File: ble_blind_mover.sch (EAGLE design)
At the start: 64 parts, among them J1 105017-0001, Q1 DMG6968U-7, Q2 DMG6968U-7, U1 MCP7940N-I/SN, U2 YJ-14015, U3 VIPER012LS, U4 MIC5205-3.3YM5-TR, Y1 LFXTAL016178

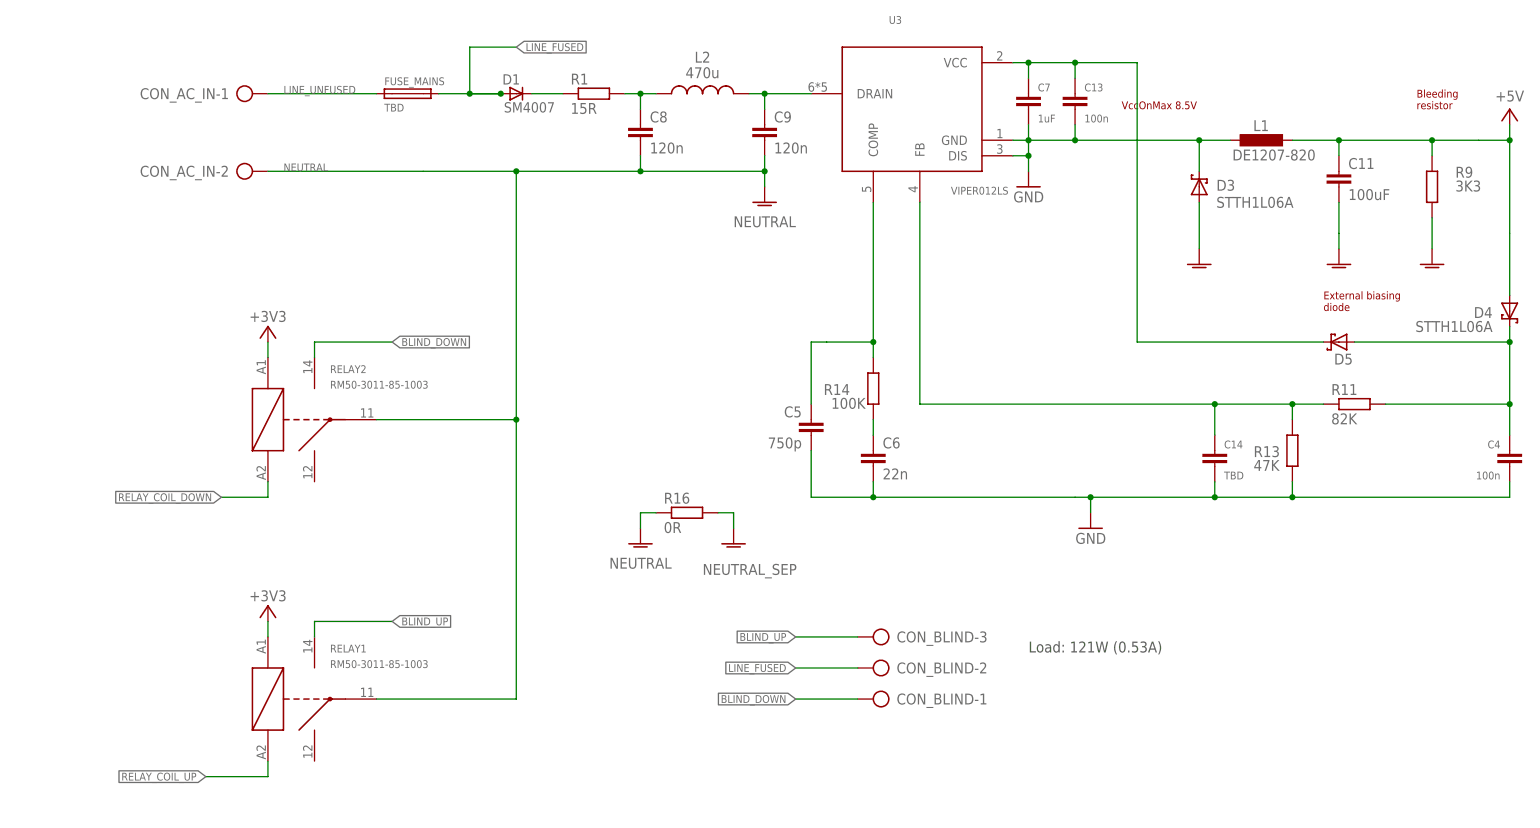
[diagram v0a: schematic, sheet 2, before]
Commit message: - Get rid from Viper PSU in favour of a Meanwell module - Make the contours to fit in a Kradex Z21 box
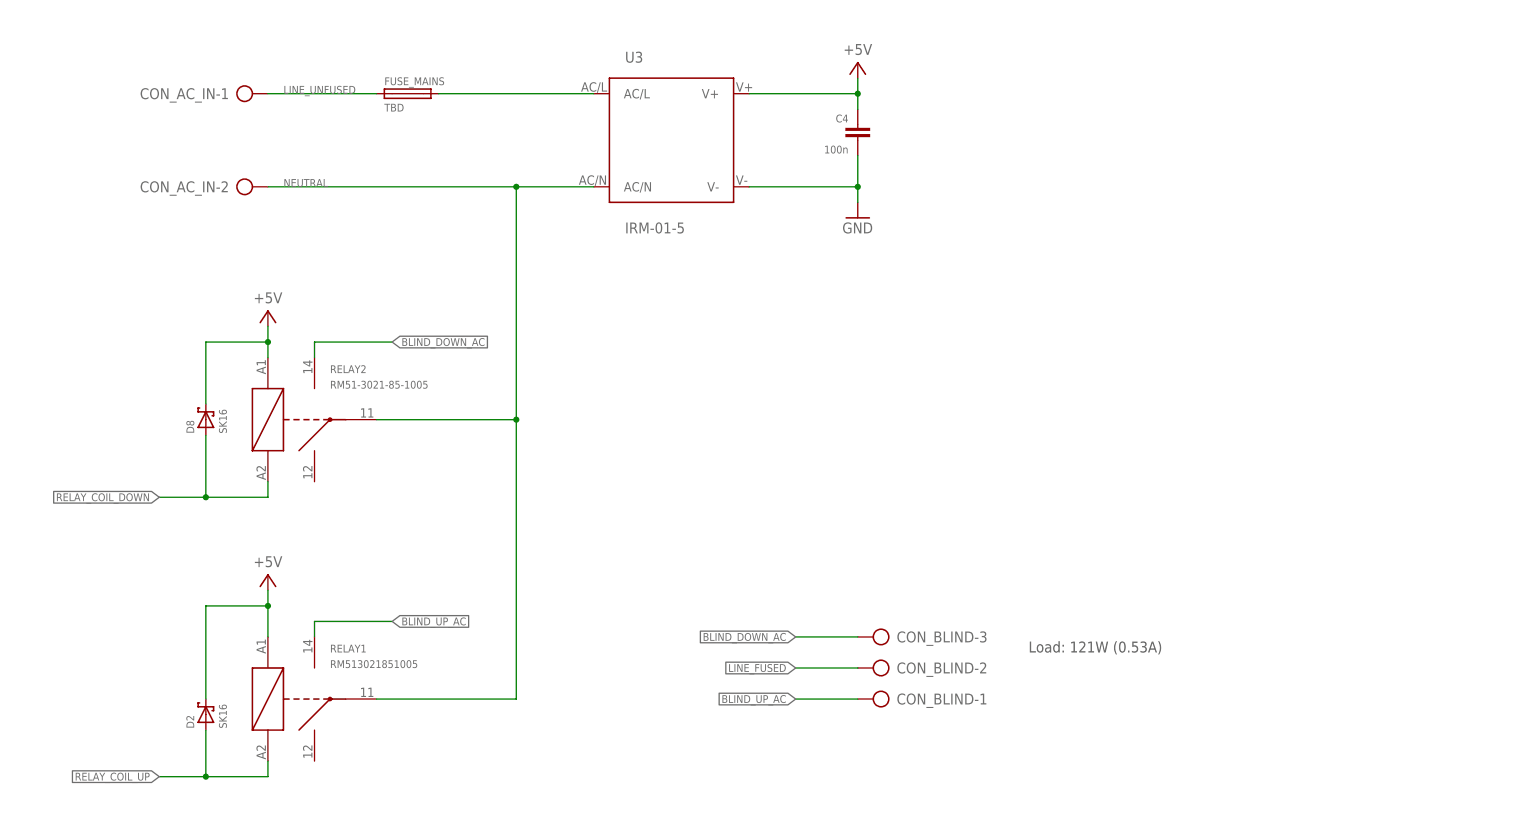
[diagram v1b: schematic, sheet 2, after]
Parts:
- removed C10, C7: 1uF, rcl:C-EUC0603
- removed C11: 100uF, rcl:C-EUC1812
- removed C13: 100n, rcl:C-EUC0603
- removed C14: TBD, rcl:C-EUC0603
- removed C5: 750p, rcl:C-EUC0603
- removed C6: 22n, rcl:C-EUC0603
- removed C8, C9: 120n, rcl:C-EU150-064X183
- removed D1: SM4007, _hhn_diodes_smd:SM4007
- removed D3, D4, D6: STTH1L06A, xCommonLib:SCHOTTKY_DIODESMA
- removed D5: (no value), diode_:SCHOTTKY-DIODESOD123
- removed J1: 105017-0001, 105017-0001:105017-0001
- removed JP1, JP2: (no value), pinhead:PINHD-1X2
- removed L1: DE1207-820, ferrocore:DE1207-820
- removed L2: 470u, SparkFun:INDUCTOR1210
- removed R1: 15R, rcl:R-EU_M1206
- removed R11: 82K, rcl:R-EU_R0603
- removed R13: 47K, rcl:R-EU_R0603
- removed R14: 100K, rcl:R-EU_R0603
- removed R16: 0R, rcl:R-EU_0207/7
- removed R9: 3K3, rcl:R-EU_R1206
- added C20, C21: 10n, rcl:C-EUC0603
- added D2, D8: SK16, diode:SCHOTTKY-DIODESK12
- added R18, R19: TBD, rcl:R-EU_R0603
- RELAY1: value RM50-3011-85-1003 -> RM513021851005; OC_TME RM50-P-03 -> RM513021851005
- RELAY2: value RM50-3011-85-1003 -> RM51-3021-85-1005; OC_TME RM50-P-03 -> RM513021851005
- U3: value VIPER012LS -> IRM-01-5; device st_viper:VIPER012LS -> meanwell_irm_v7:IRM_01/02IRM_01/02; OC_TME (none) -> IRM-01-5
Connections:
- removed net BLIND_DOWN: CON_BLIND-1.KL, RELAY2.14
- removed net BLIND_UP: CON_BLIND-3.KL, RELAY1.14
- removed net LINE_FILTERED: C9.1, L2.2, U3.DRAIN
- removed net LINE_RECTIFIED: D1.C, R1.1
- removed net LINE_RECTIFIED_R: C8.1, L2.1, R1.2
- removed net NEUTRAL_SEP: C11.2, D3.A, R16.2, R9.1
- removed net VIPER_COMP: C5.1, R14.2, U3.COMP
- removed net VIPER_COMP_MID: C6.1, R14.1
- removed net VIPER_FB: C14.1, R11.1, R13.2, U3.FB
- removed net VIPER_PRE_FB: C4.1, D4.C, D5.A, R11.2
- removed net VIPER_VCC: C13.1, C7.1, D5.C, U3.VCC
- removed net VUSB: D6.A, J1.VUSB
- new net BLIND_DOWN_AC: CON_BLIND-3.KL, RELAY2.14
- new net BLIND_UP_AC: CON_BLIND-1.KL, RELAY1.14
- new net BTN_DOWN_R: C20.1, R18.1, S4.S, S4.S1
- new net BTN_UP_R: C21.1, R19.1, S3.S, S3.S1
- net +3V3: no longer JP1.1, RELAY1.A1, RELAY2.A1
- net +5V: now also C4.1, D2.C, D8.C, RELAY1.A1, RELAY2.A1, U3.V+; no longer C10.1, C11.1, D4.A, D6.C, JP2.1, L1.2, R9.2
- net BTN_DOWN: now also R18.2, U2.P0.21; no longer S4.S, S4.S1, U2.P0.16
- net BTN_UP: now also R19.2; no longer S3.S, S3.S1
- net GND: now also C20.2, C21.2, U3.V-; no longer C10.2, C13.2, C14.2, C5.2, C6.2, C7.2, D3.C, J1.GND, J1.HOLES, J1.PADS, JP1.2, JP2.2, L1.1, R13.1, U3.DIS, U3.GND
- net LINE_FUSED: now also U3.AC/L; no longer D1.A
- net NEUTRAL: now also U3.AC/N; no longer C8.2, C9.2, R16.1
- net RELAY_COIL_DOWN: now also D8.A
- net RELAY_COIL_UP: now also D2.A
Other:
- note added: "+3V3"
- note added: "+5V"
- note added: "230V - 5V AC/DC converter"
- note added: "2x 5V Relay"
- note removed: "2 Relays"
- note removed: "230V - 3V3 AC/DC converter"
- note removed: "3V3"
- note removed: "Bleeding resistor"
- note removed: "External biasing diode"
- note removed: "PI filter, 1/2 bridge rectifier"
- note removed: "VccOnMax 8.5V"
- note removed: "uUSB socket"
- moved on the sheet: C12, C15, C17, C19, C4, CON_AC_IN-2, JP3, R15, R17, U1, Y1

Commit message: MOved to a triac based design
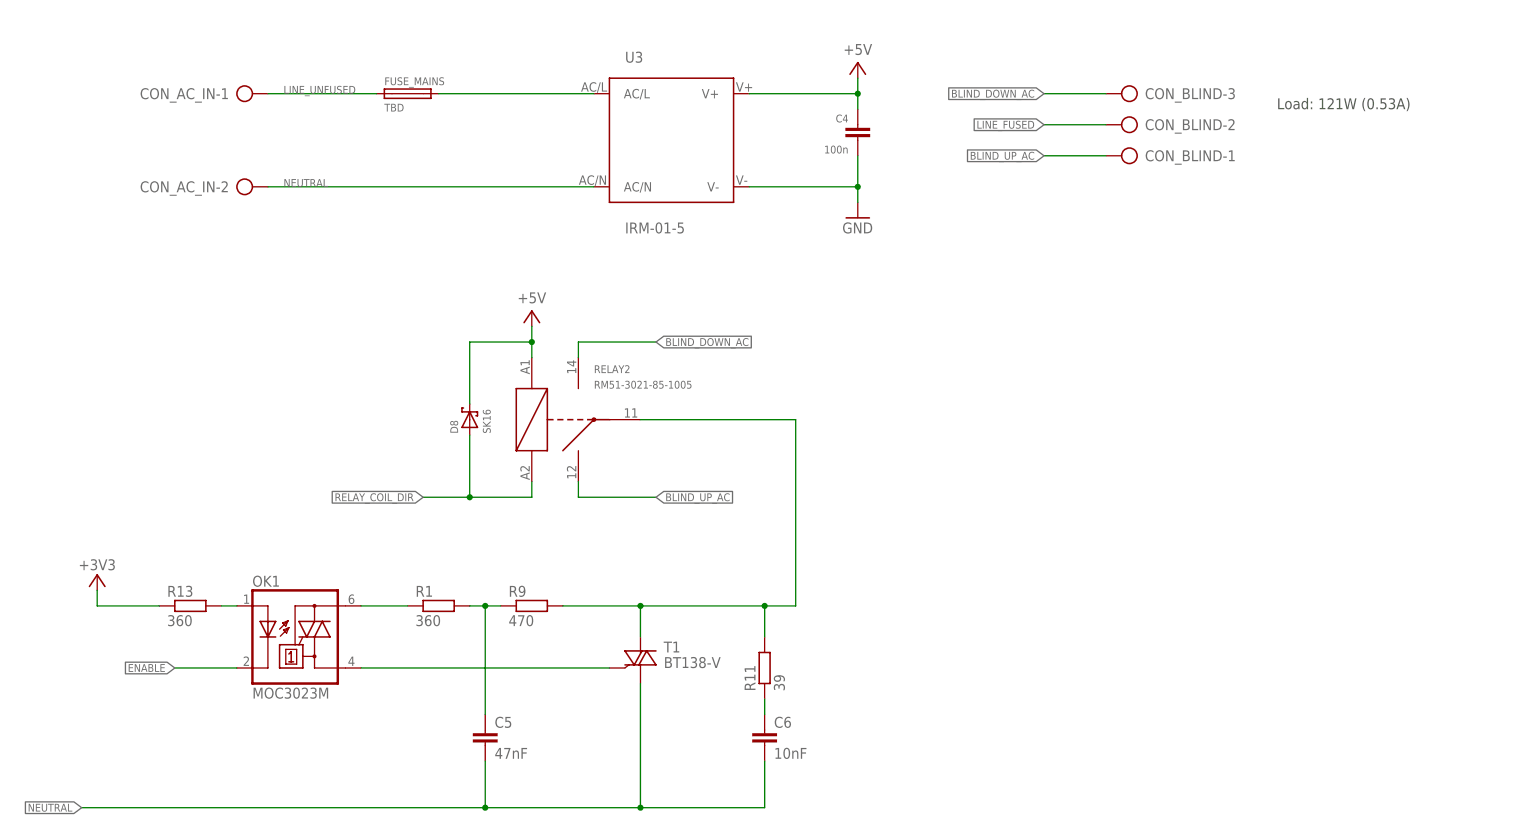
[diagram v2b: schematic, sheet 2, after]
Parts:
- removed D2: SK16, diode:SCHOTTKY-DIODESK12
- removed Q1: DMG6968U-7, SparkFun:MOSFET-NCHANNELSMD
- removed R2: 47K, rcl:R-EU_R0603
- removed R3: 10R, rcl:R-EU_R0603
- removed R6: TBD, rcl:R-EU_R0603
- removed RELAY1: RM513021851005, relay-relpol:RM50-3011-XX-XXXX
- added C5: 47nF, rcl:C-EU025-030X050
- added C6: 10nF, rcl:C-EU025-030X050
- added OK1: MOC3023M, optocoupler:MOC3023M
- added R1: 360, rcl:R-EU_R0805
- added R11: 39, rcl:R-EU_0204/2V
- added R13: 360, rcl:R-EU_R0603
- added R9: 470, rcl:R-EU_R0805
- added T1: BT138-V, triac:BT138-V
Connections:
- net GO_DOWN renamed DIRECTION
- net RELAY_COIL_DOWN renamed RELAY_COIL_DIR
- net RELAY_COIL_DOWN__R renamed RELAY_COIL_DIR_R
- removed net GO_UP: R3.1, U2.P0.12
- removed net MOTOR_A_GATE_R: Q1.G, R2.1, R3.2
- removed net RELAY_COIL_UP: D2.A, R6.2, RELAY1.A2
- removed net RELAY_COIL_UP__R: Q1.D, R6.1
- new net ENABLE: OK1.C, U2.P0.12
- new net LOAD_B: R11.2, R9.2, RELAY2.11, T1.A2
- new net MOC_AN: OK1.A, R13.2
- new net MOC_OUT: OK1.A2, R1.1
- new net N$2: C5.1, R1.2, R9.1
- new net SNUB_MID: C6.1, R11.1
- new net TRIAC_GET: OK1.A1, T1.G
- net +3V3: now also R13.1
- net +5V: no longer D2.C, RELAY1.A1
- net BLIND_UP_AC: now also RELAY2.12; no longer RELAY1.14
- net GND: no longer Q1.S, R2.2
- net NEUTRAL: now also C5.2, C6.2, T1.A1; no longer RELAY1.11, RELAY2.11
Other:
- note added: "Direction relay"
- note added: "Enable optotriac"
- note added: "enable"
- note removed: "2x 5V Relay"
- moved on the sheet: CON_BLIND-1, CON_BLIND-2, CON_BLIND-3, D8, RELAY2

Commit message: Added B2B connector for I2C
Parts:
- added JP1: (no value), pinhead:PINHD-2X2
- added R2: TBD, rcl:R-EU_R0603
- renumbered RELAY2 to RELAY1
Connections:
- net +3V3: now also JP1.4
- net ENABLE: now also R2.2
- net GND: now also JP1.2
- net MOC_AN: now also R2.1
- net SCL: now also JP1.1
- net SDA: now also JP1.3
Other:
- moved on the sheet: R13
